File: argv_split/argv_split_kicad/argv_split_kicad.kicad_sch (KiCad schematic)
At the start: 162 parts, among them SW1 F1, SW10 F10, SW11 F11, SW12 F12, SW13 Caps, SW14 1, SW15 2, SW16 3, SW17 4, SW18 5, SW19 (, SW2 F2, SW20 ), SW21 6, SW22 7, SW23 8, SW24 9, SW25 0, SW26 Fn, SW27 Tab, SW28 Q, SW29 W, SW3 F3, SW30 E, SW31 R, SW32 T, SW33 {, SW34 }, SW35 Y, SW36 U, SW37 I, SW38 O, SW39 P, SW4 F4, SW40 =, SW41 Esc, SW42 A, SW43 S, SW44 D, SW45 F, SW46 G, SW47 [, SW48 ], SW49 H, SW5 F5, SW50 J, SW51 K, SW52 L, SW53 ;, SW54 -, SW55 Shift, SW56 Z, SW57 X, SW58 C, SW59 V, SW6 F6, SW60 B, SW61 ', SW62 ", SW63 N, SW64 M, SW65 ,, SW66 ., SW67 "/", SW68 RShift, SW69 Space, SW7 F7, SW70 Backspace, SW71 Left, SW72 Down, SW73 Up, SW74 Right, SW75 Ctrl, SW76 Linux, SW77 alt, SW78 Return, SW79 Linux, SW8 F8, SW80 Ctrl, SW9 F9

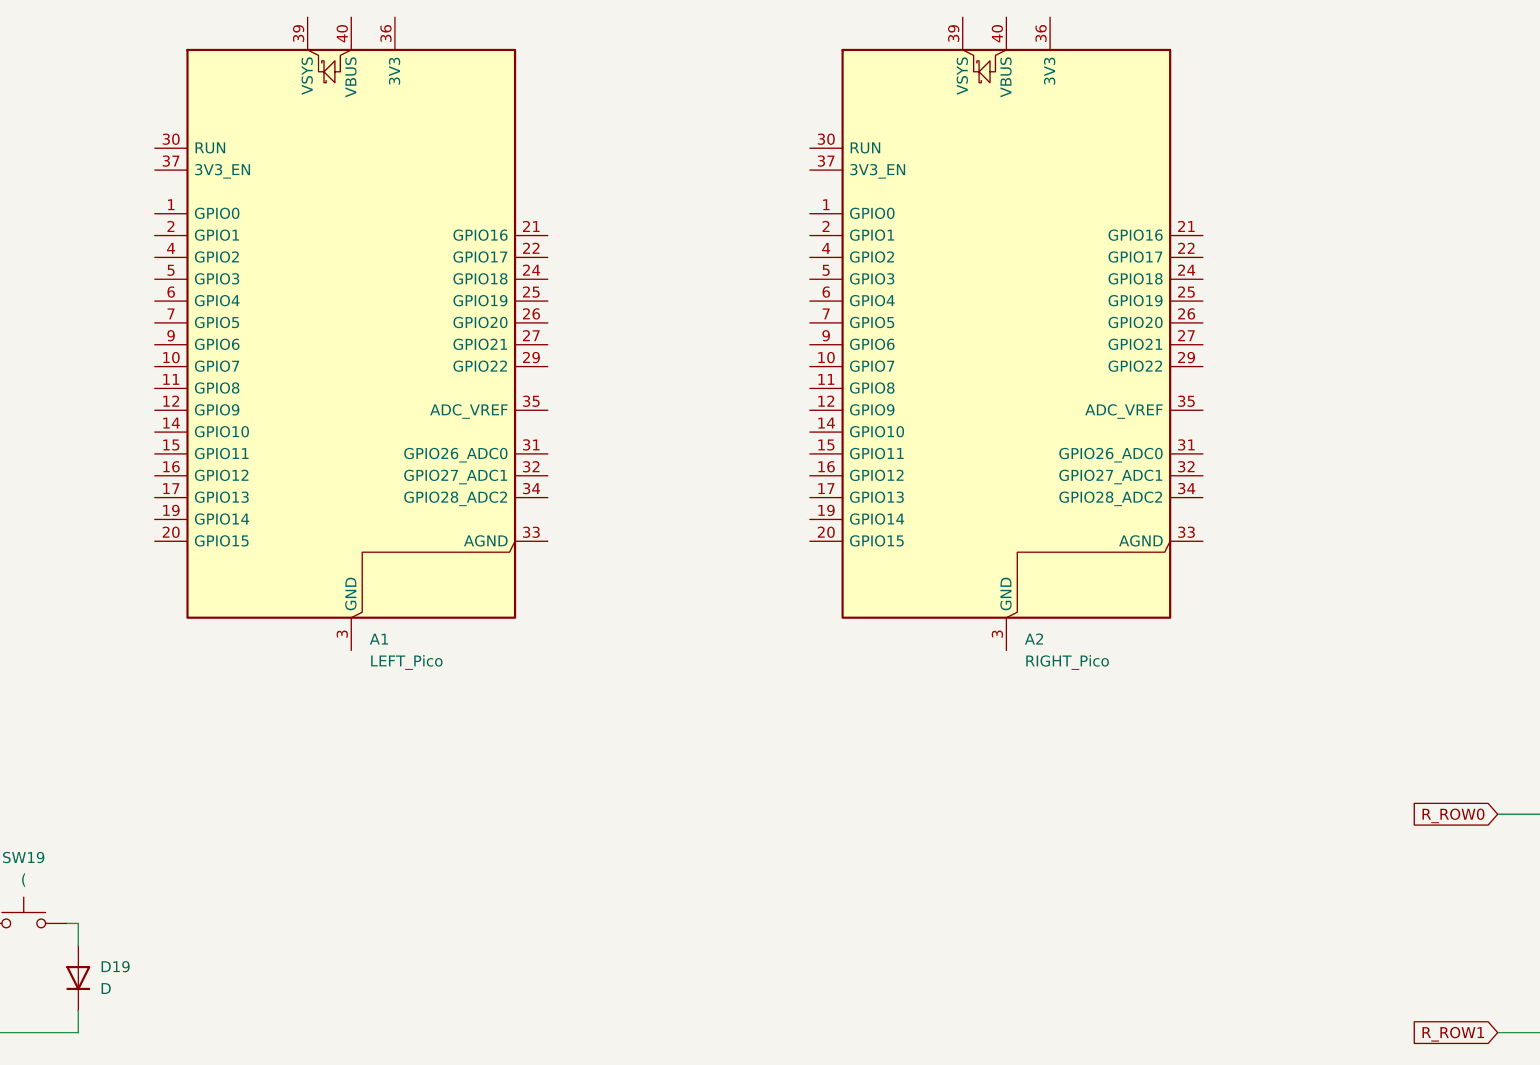
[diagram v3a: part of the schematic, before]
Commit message: feat(split): schematics layout
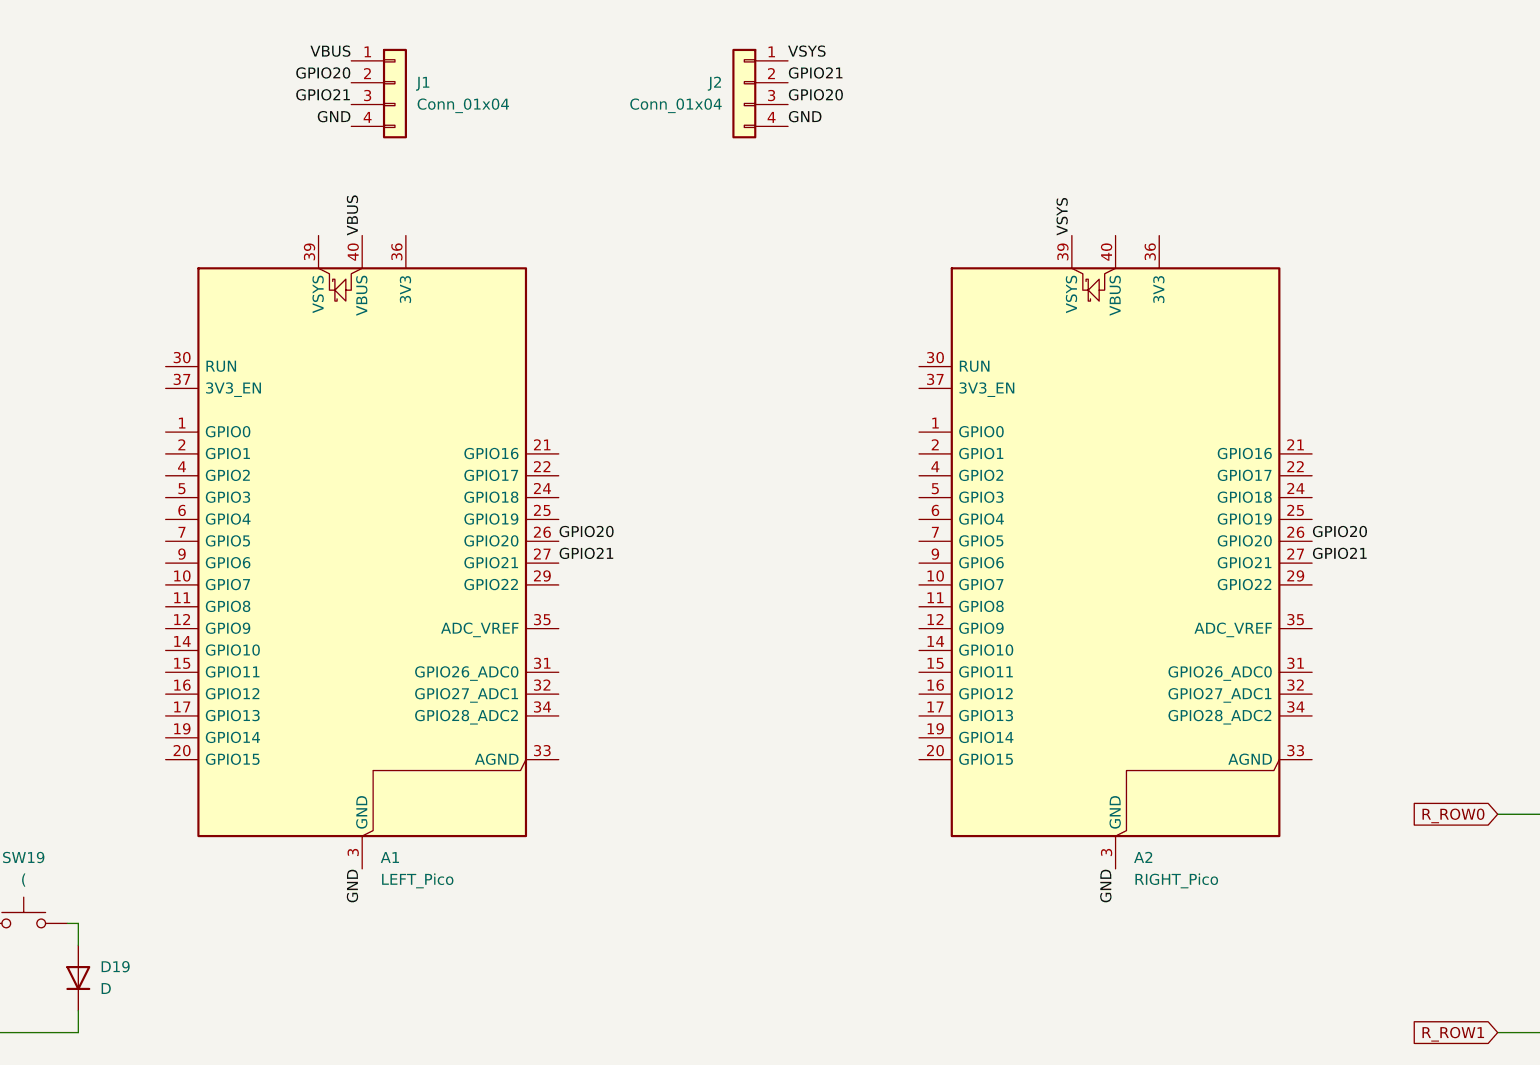
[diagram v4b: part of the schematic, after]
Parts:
- added J1, J2: Conn_01x04, symbol Connector_Generic:Conn_01x04
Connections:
- net GND: now reaches A2.13 (GND), A2.18 (GND), A2.23 (GND), A2.28 (GND), A2.3 (GND), A2.38 (GND), A2.8 (GND)
- net GND: now also A1.13 (GND), A1.18 (GND), A1.23 (GND), A1.28 (GND), A1.3 (GND), A1.38 (GND), A1.8 (GND), J1.4 (Pin_4), J2.4 (Pin_4)
- net GPIO20: now reaches A2.26 (GPIO20)
- net GPIO20: now also A1.26 (GPIO20), J1.2 (Pin_2), J2.3 (Pin_3)
- net GPIO21: now reaches A2.27 (GPIO21)
- net GPIO21: now also A1.27 (GPIO21), J1.3 (Pin_3), J2.2 (Pin_2)
- net VSYS: now reaches A2.39 (VSYS)
- net VSYS: now also J2.1 (Pin_1)
- net VBUS: now reaches A1.40 (VBUS)
- net VBUS: now also J1.1 (Pin_1)
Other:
- moved on the sheet: A1, A2

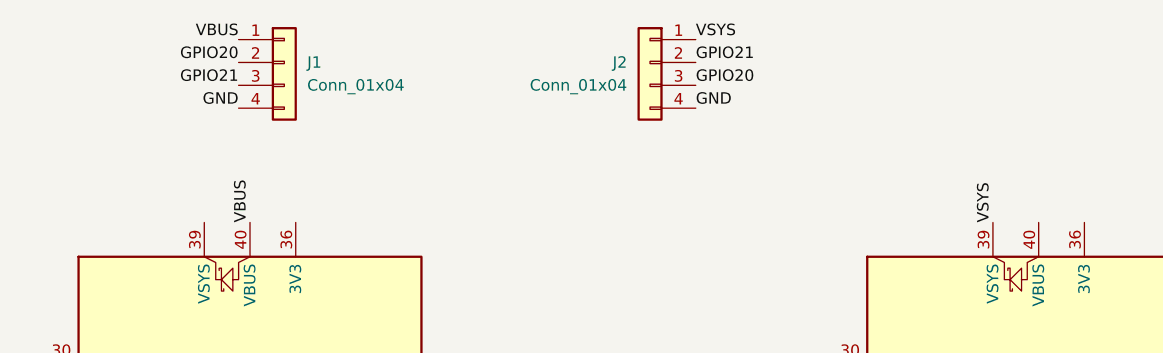
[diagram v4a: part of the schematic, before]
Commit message: fix(split): switch sizes
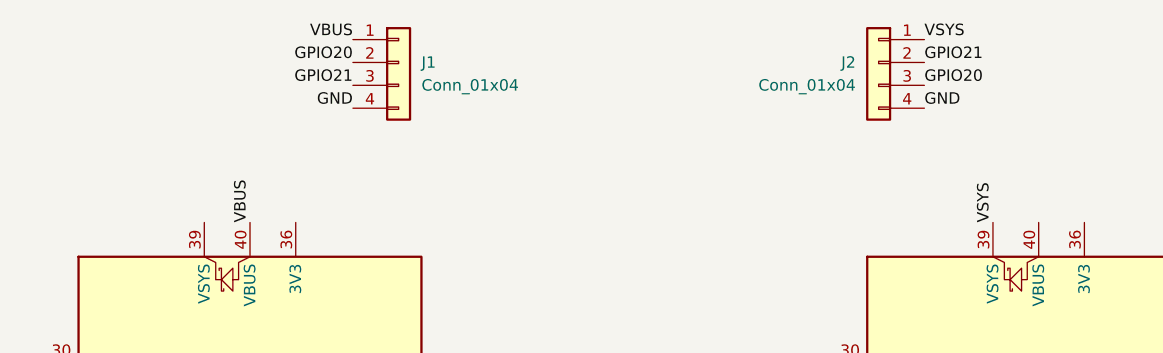
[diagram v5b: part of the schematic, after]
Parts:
- J1, J2: footprint (none) -> Connector_PinHeader_2.54mm:PinHeader_1x04_P2.54mm_Vertical
- SW75, SW76, SW77, SW78, SW79, SW80: footprint PCM_Switch_Keyboard_Hotswap_Kailh:SW_Hotswap_Kailh_MX_2.00u -> PCM_Switch_Keyboard_Hotswap_Kailh:SW_Hotswap_Kailh_MX_2.00u_90deg
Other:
- moved on the sheet: J1, J2
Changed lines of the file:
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@@
 	)
 	(label "GPIO20"
-		(at 247.65 29.21 180)
+		(at 260.35 29.21 180)
 		(effects
 			(font
@@
 	)
 	(label "VBUS"
-		(at 247.65 26.67 180)
+		(at 260.35 26.67 180)
 		(effects
 			(font
@@
 	)
 	(label "GPIO21"
-		(at 247.65 31.75 180)
+		(at 260.35 31.75 180)
 		(effects
 			(font
@@
 	)
 	(label "GPIO21"
-		(at 298.45 29.21 0)
+		(at 323.85 29.21 0)
 		(effects
 			(font
@@
 	)
 	(label "GPIO20"
-		(at 298.45 31.75 0)
+		(at 323.85 31.75 0)
 		(effects
 			(font
@@
 	)
 	(label "GND"
-		(at 298.45 34.29 0)
+		(at 323.85 34.29 0)
 		(effects
 			(font
@@
 	)
 	(label "GND"
-		(at 247.65 34.29 180)
+		(at 260.35 34.29 180)
 		(effects
 			(font
@@
 	)
 	(label "VSYS"
-		(at 298.45 26.67 0)
+		(at 323.85 26.67 0)
 		(effects
 			(font
@@
 			)
 		)
-		(property "Footprint" "PCM_Switch_Keyboard_Hotswap_Kailh:SW_Hotswap_Kailh_MX_2.00u"
+		(property "Footprint" "PCM_Switch_Keyboard_Hotswap_Kailh:SW_Hotswap_Kailh_MX_2.00u_90deg"
 			(at 184.15 261.62 0)
 			(hide yes)
@@
 	(symbol
 		(lib_id "Connector_Generic:Conn_01x04")
-		(at 293.37 29.21 0)
+		(at 318.77 29.21 0)
 		(mirror y)
 		(unit 1)
@@
 		(dnp no)
 		(property "Reference" "J2"
-			(at 290.83 29.2099 0)
+			(at 316.23 29.2099 0)
 			(show_name no)
 			(do_not_autoplace no)
@@
 		)
 		(property "Value" "Conn_01x04"
-			(at 290.83 31.7499 0)
+			(at 316.23 31.7499 0)
 			(show_name no)
 			(do_not_autoplace no)
@@
 			)
 		)
-		(property "Footprint" ""
-			(at 293.37 29.21 0)
+		(property "Footprint" "Connector_PinHeader_2.54mm:PinHeader_1x04_P2.54mm_Vertical"
+			(at 318.77 29.21 0)
 			(hide yes)
 			(show_name no)
@@
 		)
 		(property "Datasheet" ""
-			(at 293.37 29.21 0)
+			(at 318.77 29.21 0)
 			(hide yes)
 			(show_name no)
@@
 		)
 		(property "Description" "Generic connector, single row, 01x04, script generated (kicad-library-utils/schlib/autogen/connector/)"
-			(at 293.37 29.21 0)
+			(at 318.77 29.21 0)
 			(hide yes)
 			(show_name no)
@@
 			)
 		)
-		(property "Footprint" "PCM_Switch_Keyboard_Hotswap_Kailh:SW_Hotswap_Kailh_MX_2.00u"
+		(property "Footprint" "PCM_Switch_Keyboard_Hotswap_Kailh:SW_Hotswap_Kailh_MX_2.00u_90deg"
 			(at 425.45 261.62 0)
 			(hide yes)
@@
 			)
 		)
-		(property "Footprint" "PCM_Switch_Keyboard_Hotswap_Kailh:SW_Hotswap_Kailh_MX_2.00u"
+		(property "Footprint" "PCM_Switch_Keyboard_Hotswap_Kailh:SW_Hotswap_Kailh_MX_2.00u_90deg"
 			(at 234.95 261.62 0)
 			(hide yes)
@@
 			)
 		)
-		(property "Footprint" "PCM_Switch_Keyboard_Hotswap_Kailh:SW_Hotswap_Kailh_MX_2.00u"
+		(property "Footprint" "PCM_Switch_Keyboard_Hotswap_Kailh:SW_Hotswap_Kailh_MX_2.00u_90deg"
 			(at 209.55 261.62 0)
 			(hide yes)
@@
 			)
 		)
-		(property "Footprint" "PCM_Switch_Keyboard_Hotswap_Kailh:SW_Hotswap_Kailh_MX_2.00u"
+		(property "Footprint" "PCM_Switch_Keyboard_Hotswap_Kailh:SW_Hotswap_Kailh_MX_2.00u_90deg"
 			(at 400.05 261.62 0)
 			(hide yes)
@@
 			)
 		)
-		(property "Footprint" "PCM_Switch_Keyboard_Hotswap_Kailh:SW_Hotswap_Kailh_MX_2.00u"
+		(property "Footprint" "PCM_Switch_Keyboard_Hotswap_Kailh:SW_Hotswap_Kailh_MX_2.00u_90deg"
 			(at 374.65 261.62 0)
 			(hide yes)
@@
 	(symbol
 		(lib_id "Connector_Generic:Conn_01x04")
-		(at 252.73 29.21 0)
+		(at 265.43 29.21 0)
 		(unit 1)
 		(body_style 1)
@@
 		(fields_autoplaced yes)
 		(property "Reference" "J1"
-			(at 255.27 29.2099 0)
+			(at 267.97 29.2099 0)
 			(show_name no)
 			(do_not_autoplace no)
@@
 		)
 		(property "Value" "Conn_01x04"
-			(at 255.27 31.7499 0)
+			(at 267.97 31.7499 0)
 			(show_name no)
 			(do_not_autoplace no)
@@
 			)
 		)
-		(property "Footprint" ""
-			(at 252.73 29.21 0)
+		(property "Footprint" "Connector_PinHeader_2.54mm:PinHeader_1x04_P2.54mm_Vertical"
+			(at 265.43 29.21 0)
 			(hide yes)
 			(show_name no)
@@
 		)
 		(property "Datasheet" ""
-			(at 252.73 29.21 0)
+			(at 265.43 29.21 0)
 			(hide yes)
 			(show_name no)
@@
 		)
 		(property "Description" "Generic connector, single row, 01x04, script generated (kicad-library-utils/schlib/autogen/connector/)"
-			(at 252.73 29.21 0)
+			(at 265.43 29.21 0)
 			(hide yes)
 			(show_name no)

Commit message: feat: starting pcb layout
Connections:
- net L_COL7 is gone; now on net L_COL6: SW69.1, SW77.1
- net L_ROW4 is gone; now on net L_COL6: D55.1 (K), D56.1 (K), D57.1 (K), D58.1 (K), D59.1 (K), D60.1 (K), D61.1 (K)
- net L_COL4: now also SW75.1
- net L_COL5: now also SW76.1; no longer SW75.1
- net L_COL6: no longer SW76.1

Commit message: revert: starting pcb layout
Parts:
- J1, J2: now not fitted
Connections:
- net L_COL0: now also A1.1 (GPIO0)
- net L_COL1: now also A1.2 (GPIO1)
- net L_COL2: now also A1.4 (GPIO2)
- net L_COL3: now also A1.5 (GPIO3)
- net L_COL4: now also A1.6 (GPIO4)
- net L_COL5: now also A1.7 (GPIO5)
- net L_COL6: now also A1.15 (GPIO11), A1.9 (GPIO6)
- net L_ROW0: now also A1.10 (GPIO7)
- net L_ROW1: now also A1.11 (GPIO8)
- net L_ROW2: now also A1.12 (GPIO9)
- net L_ROW3: now also A1.14 (GPIO10)
- net L_ROW5: now also A1.16 (GPIO12)
- net L_ROW6: now also A1.17 (GPIO13)

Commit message: feat: pcb layout
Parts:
- D1, D10, D11, D12, D13, D14, D15, D16, D17, D18, D19, D2, D20, D21, D22, D23, D24, D25, D26, D27, D28, D29, D3, D30, D31, D32, D33, D34, D35, D36, D37, D38, D39, D4, D40, D41, D42, D43, D44, D45, D46, D47, D48, D49, D5, D50, D51, D52, D53, D54, D55, D56, D57, D58, D59, D6, D60, D61, D62, D63, D64, D65, D66, D67, D68, D69, D7, D70, D71, D72, D73, D74, D75, D76, D77, D78, D79, D8, D80, D9: footprint Diode_THT:D_DO-35_SOD27_P7.62mm_Horizontal -> Diode_THT:D_DO-35_SOD27_P5.08mm_Vertical_AnodeUp
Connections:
- net GPIO20: now also J1.3 (Pin_3), J2.2 (Pin_2); no longer J1.2 (Pin_2), J2.3 (Pin_3)
- net GPIO21: now also J1.2 (Pin_2), J2.3 (Pin_3); no longer J1.3 (Pin_3), J2.2 (Pin_2)
- net L_ROW5: now also A1.17 (GPIO13); no longer A1.16 (GPIO12)
- net L_ROW6: now also A1.16 (GPIO12); no longer A1.17 (GPIO13)
